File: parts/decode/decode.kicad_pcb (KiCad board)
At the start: 2 copper layers, 37 parts, among them J1 Conn_02x02_Odd_Even, J10 Conn_01x02, J11 Conn_01x02, J12 Conn_01x02, J13 Conn_01x02, J14 Conn_02x04_Odd_Even, J2 Conn_02x04_Odd_Even, J3 Conn_01x02, J4 Conn_01x02, J5 Conn_01x02, J6 Conn_01x02, J7 Conn_01x02, J8 Conn_01x02, J9 Conn_01x02, K1 HK19F, K10 HK19F, K11 HK19F, K2 HK19F, K3 HK19F, K4 HK19F, K5 HK19F, K6 HK19F, K7 HK19F, K8 HK19F, K9 HK19F

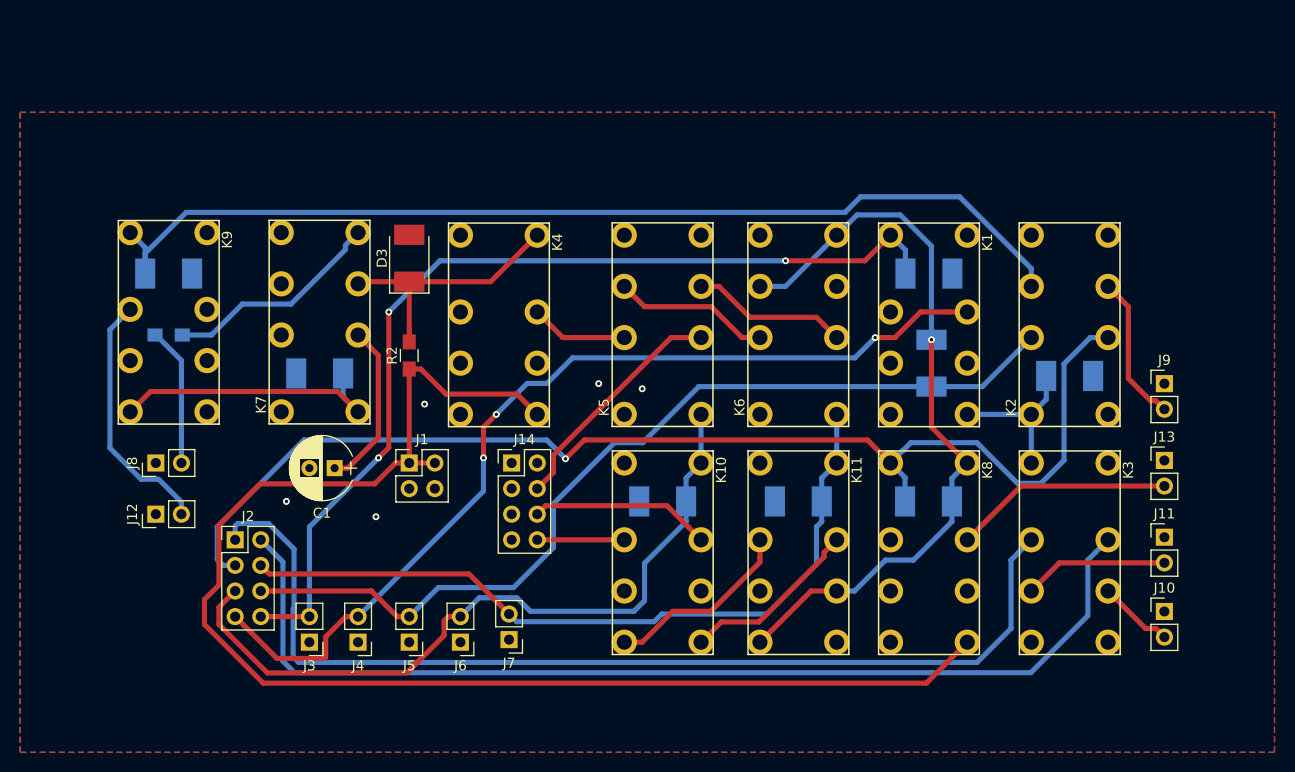
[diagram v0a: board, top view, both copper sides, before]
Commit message: Change opcodes (jumps from rediscovered notes).
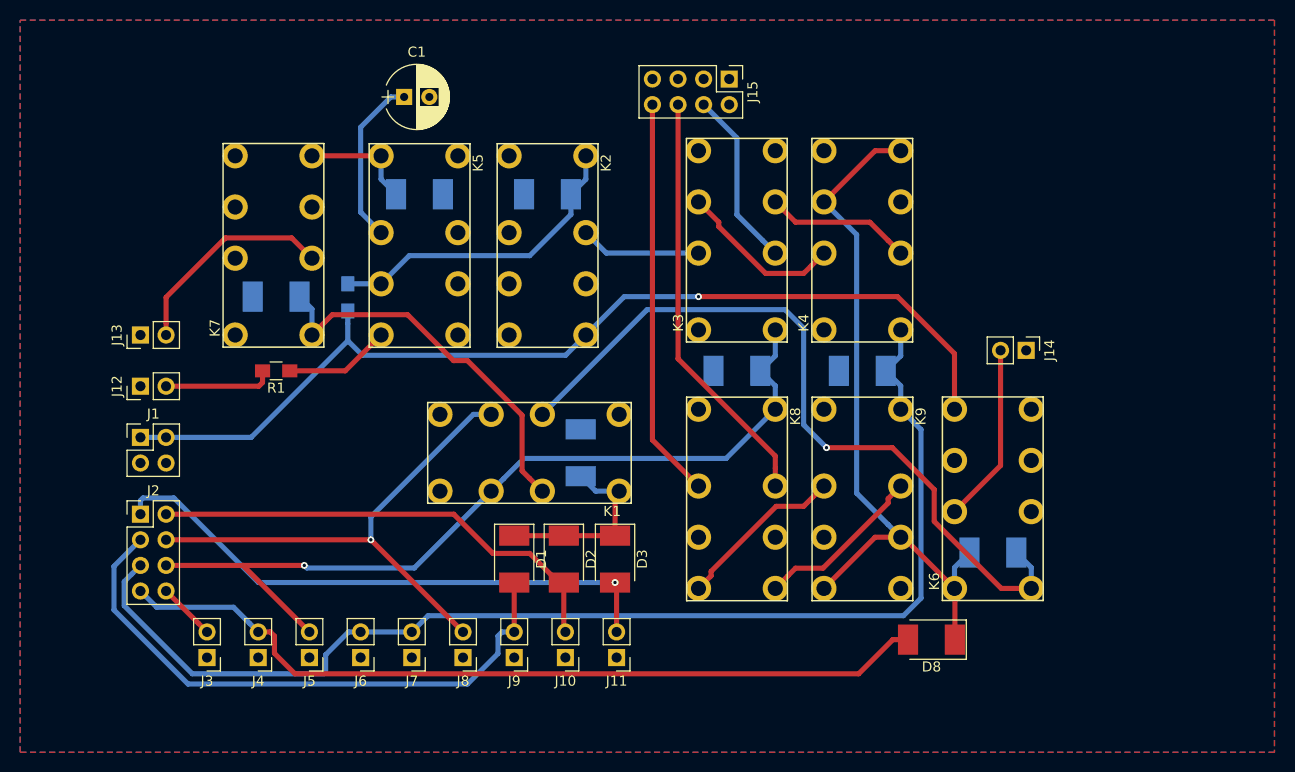
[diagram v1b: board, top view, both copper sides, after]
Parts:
- removed K10, K11: HK19F, hk19f:Relay_DPDT_HK19F
- added D10: D, Diodes_SMD:D_2114, B.Cu at (159.0, 71.6)
- added D11: D, Diodes_SMD:D_2114, B.Cu at (144.8, 81.8)
- added J15: Conn_02x04_Odd_Even, Pin_Headers:Pin_Header_Straight_2x04_Pitch2.54mm, F.Cu at (189.7, 60.2)
- D1, D2, D8, R1: moved to F.Cu
- D7: value D_TVS -> D
- D9: value D -> D_TVS
- J14: value Conn_02x04_Odd_Even -> Conn_01x02; footprint Pin_Headers:Pin_Header_Straight_2x04_Pitch2.54mm -> Pin_Headers:Pin_Header_Straight_1x02_Pitch2.54mm
- R2: moved to B.Cu
- moved J13 102.4 mm to (131.3, 85.6), turned to 90 degrees
- moved D9 86.3 mm to (215.9, 107.2)
- moved K9 71.0 mm to (206.8, 93.0)
- moved J9 70.0 mm to (168.4, 117.6), turned to 180 degrees
- moved D8 66.2 mm to (209.8, 115.8)
- moved J10 59.6 mm to (173.5, 117.6), turned to 180 degrees
- moved J11 55.7 mm to (178.6, 117.6), turned to 180 degrees
- moved D2 53.4 mm to (173.3, 107.8), turned to 270 degrees
- moved J14 52.3 mm to (219.2, 87.1), turned to 270 degrees
- moved K2 51.1 mm to (175.5, 67.8), turned to 270 degrees
- moved D1 50.0 mm to (168.4, 107.8), turned to 270 degrees
- moved K1 42.9 mm to (178.8, 101.1), turned to 180 degrees
- moved K3 42.7 mm to (186.7, 85.1), turned to 90 degrees
- moved D5 39.4 mm to (171.7, 71.6)
- moved C1 37.5 mm to (157.5, 62.0), turned to 0 degrees
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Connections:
- D1 pad 2: GND -> Net-(D1-Pad2)
- D2 pad 1: Net-(D2-Pad1) -> Net-(D1-Pad1)
- D2 pad 2: GND -> Net-(D2-Pad2)
- D3 pad 1: Net-(D3-Pad1) -> Net-(D1-Pad1)
- D3 pad 2: GND -> Net-(D3-Pad2)
- D4 pad 1: Net-(D4-Pad1) -> Net-(D1-Pad1)
- D6 pad 2: Net-(D6-Pad2) -> GND
- D7 pad 1: Net-(D6-Pad1) -> Net-(D7-Pad1)
- D7 pad 2: Net-(D7-Pad2) -> GND
- D8 pad 2: GND -> Net-(D8-Pad2)
- D9 pad 1: Net-(D9-Pad1) -> Net-(D8-Pad1)
- D9 pad 2: GND -> Net-(D9-Pad2)
- J10 pad 2: Net-(J10-Pad2) -> Net-(D2-Pad2)
- J11 pad 2: Net-(J11-Pad2) -> Net-(D3-Pad2)
- J14 pad 2: (no net) -> Net-(J14-Pad2)
- J2 pad 1: Net-(J2-Pad1) -> Net-(D3-Pad2)
- J2 pad 2: Net-(J2-Pad2) -> Net-(D2-Pad2)
- J2 pad 3: Net-(D7-Pad2) -> Net-(D1-Pad2)
- J2 pad 4: Net-(D5-Pad1) -> Net-(J2-Pad4)
- J2 pad 5: Net-(D4-Pad1) -> Net-(D7-Pad1)
- J2 pad 6: Net-(D6-Pad2) -> Net-(D6-Pad1)
- J2 pad 7: Net-(J2-Pad7) -> Net-(D8-Pad2)
- J2 pad 8: Net-(D1-Pad1) -> Net-(J2-Pad8)
- J3 pad 2: Net-(D1-Pad1) -> Net-(J2-Pad8)
- J4 pad 2: Net-(J2-Pad7) -> Net-(D8-Pad2)
- J5 pad 2: Net-(D6-Pad2) -> Net-(D6-Pad1)
- J6 pad 2: Net-(D4-Pad1) -> Net-(D7-Pad1)
- J7 pad 2: Net-(D5-Pad1) -> Net-(D7-Pad1)
- J8 pad 2: Net-(J8-Pad2) -> Net-(J2-Pad4)
- J9 pad 2: Net-(J9-Pad2) -> Net-(D1-Pad2)
- K1 pad 1: GND -> Net-(D1-Pad1)
- K1 pad 11: (no net) -> Net-(J2-Pad4)
- K1 pad 13: (no net) -> Net-(D9-Pad2)
- K1 pad 16: Net-(D1-Pad1) -> GND
- K1 pad 4: Net-(J2-Pad7) -> Net-(D11-Pad1)
- K1 pad 6: (no net) -> Net-(D6-Pad1)
- K1 pad 8: Net-(D2-Pad1) -> (no net)
- K2 pad 1: Net-(D2-Pad1) -> Net-(D5-Pad1)
- K2 pad 11: Net-(J9-Pad2) -> (no net)
- K2 pad 13: Net-(D7-Pad2) -> (no net)
- K2 pad 4: Net-(D6-Pad2) -> Net-(K2-Pad4)
- K2 pad 6: Net-(D9-Pad1) -> GND
- K2 pad 8: (no net) -> +12V
- K3 pad 11: Net-(J11-Pad2) -> Net-(K3-Pad11)
- K3 pad 13: Net-(J2-Pad1) -> Net-(J15-Pad4)
- K3 pad 16: Net-(D2-Pad1) -> Net-(D6-Pad1)
- K3 pad 4: Net-(J2-Pad2) -> Net-(K2-Pad4)
- K3 pad 6: Net-(J10-Pad2) -> Net-(K3-Pad6)
- K4 pad 1: Net-(D3-Pad1) -> GND
- K4 pad 13: (no net) -> Net-(K3-Pad11)
- K4 pad 16: GND -> Net-(D7-Pad1)
- K4 pad 4: Net-(K4-Pad4) -> Net-(K3-Pad6)
- K4 pad 6: GND -> Net-(D8-Pad1)
- K4 pad 8: +12V -> (no net)
- K4 pad 9: (no net) -> Net-(D8-Pad1)
- K5 pad 11: Net-(K5-Pad11) -> Net-(D5-Pad1)
- K5 pad 13: Net-(J14-Pad4) -> Net-(C1-Pad1)
- K5 pad 16: Net-(D4-Pad1) -> Net-(D10-Pad1)
- K5 pad 4: Net-(K4-Pad4) -> (no net)
- K5 pad 6: Net-(K5-Pad6) -> (no net)
- K5 pad 9: (no net) -> Net-(K5-Pad9)
- K6 pad 1: GND -> Net-(D8-Pad1)
- K6 pad 13: Net-(K5-Pad11) -> (no net)
- K6 pad 16: Net-(D5-Pad1) -> Net-(D9-Pad2)
- K6 pad 4: Net-(K5-Pad6) -> Net-(J14-Pad2)
- K6 pad 6: Net-(D6-Pad1) -> GND
- K6 pad 8: (no net) -> +12V
- K6 pad 9: Net-(D6-Pad1) -> (no net)
- K7 pad 11: Net-(D3-Pad1) -> (no net)
- K7 pad 13: Net-(C1-Pad1) -> Net-(J13-Pad2)
- K7 pad 16: Net-(D8-Pad1) -> Net-(D11-Pad1)
- K7 pad 9: Net-(K7-Pad9) -> Net-(D10-Pad1)
- K8 pad 13: (no net) -> Net-(J15-Pad8)
- K8 pad 16: Net-(D7-Pad2) -> GND
- K8 pad 4: Net-(J13-Pad2) -> Net-(J15-Pad6)
- K8 pad 6: GND -> (no net)
- K8 pad 8: +12V -> Net-(K8-Pad8)
- K8 pad 9: (no net) -> Net-(K8-Pad9)
- K9 pad 1: GND -> Net-(D7-Pad1)
- K9 pad 13: Net-(J12-Pad2) -> Net-(K8-Pad9)
- K9 pad 16: Net-(D9-Pad1) -> GND
- K9 pad 4: (no net) -> Net-(K8-Pad8)
- K9 pad 6: (no net) -> Net-(D8-Pad1)
- R1 pad 1: Net-(K7-Pad9) -> Net-(K5-Pad9)
- R1 pad 2: Net-(J8-Pad2) -> Net-(J12-Pad2)
- R2 pad 2: Net-(D3-Pad1) -> Net-(D5-Pad1)
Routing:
- net Net-(D7-Pad1): track 0.00 -> 119.3 mm
- net Net-(D7-Pad2): track 118.2 -> 0.00 mm, vias 1 -> 0
- net Net-(J2-Pad2): track 104.0 -> 0.00 mm
- net Net-(D9-Pad1): track 101.7 -> 0.00 mm
- net Net-(J2-Pad1): track 101.6 -> 0.00 mm
- net Net-(J2-Pad7): track 93.5 -> 0.00 mm, vias 3 -> 0
- net Net-(D6-Pad2): track 91.5 -> 0.00 mm
- net Net-(D8-Pad2): track 0.00 -> 82.0 mm
- net Net-(D1-Pad1): track 95.7 -> 19.0 mm, vias 3 -> 0
- net Net-(D9-Pad2): track 0.00 -> 75.9 mm, vias 0 -> 1
- net Net-(D4-Pad1): track 74.0 -> 0.00 mm
- net Net-(D1-Pad2): track 0.00 -> 58.9 mm
- net Net-(D3-Pad2): track 0.00 -> 57.0 mm, vias 0 -> 1
- net Net-(J2-Pad4): track 0.00 -> 51.7 mm, vias 0 -> 1
- net Net-(D2-Pad2): track 0.00 -> 47.2 mm
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
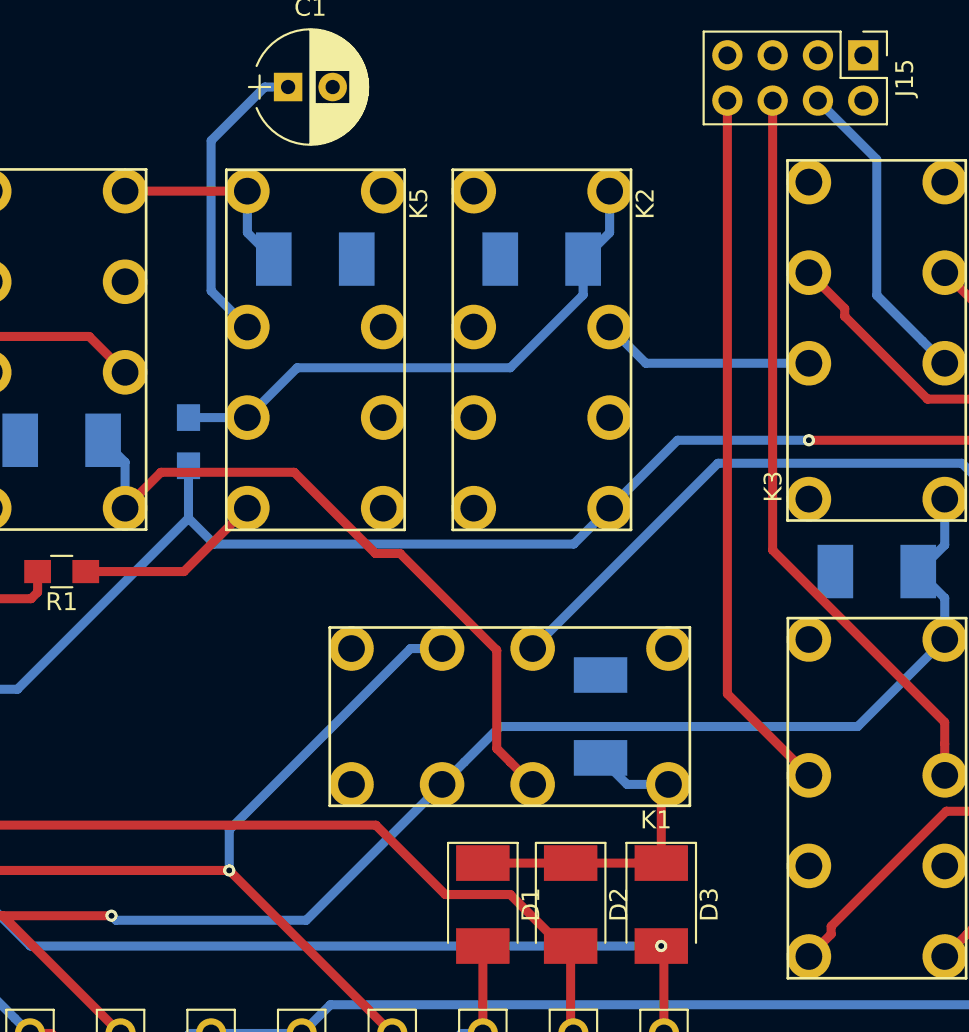
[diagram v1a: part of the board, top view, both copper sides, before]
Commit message: Git-ignore (old) parts directory, commit final changes there.
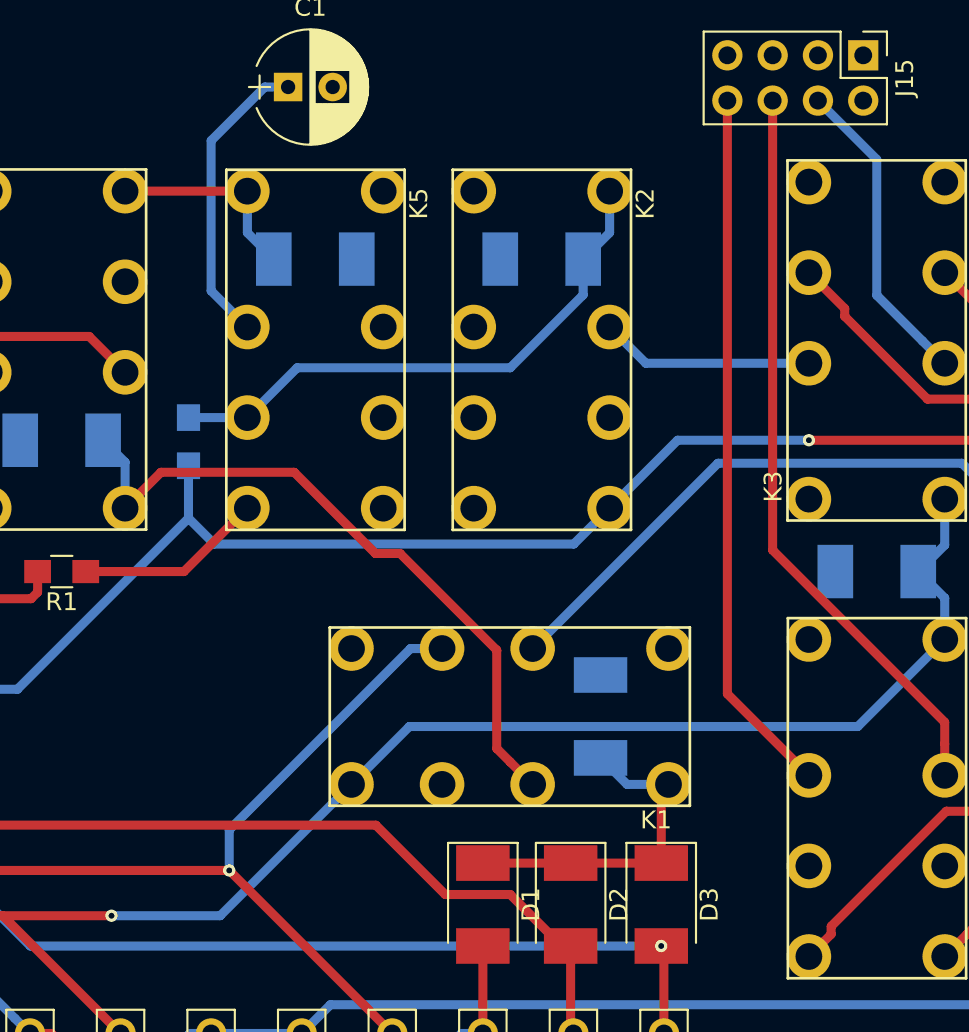
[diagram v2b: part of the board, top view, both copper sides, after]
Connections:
- D6 pad 1: Net-(D6-Pad1) -> Net-(D6-K)
- J15 pad 2: (no net) -> unconnected-(J15-Pin_2-Pad2)
- J2 pad 6: Net-(D6-Pad1) -> Net-(D6-K)
- J5 pad 2: Net-(D6-Pad1) -> Net-(D6-K)
- K1 pad 6: Net-(D6-Pad1) -> unconnected-(K1-Pad6)
- K1 pad 8: (no net) -> Net-(D6-K)
- K1 pad 9: (no net) -> unconnected-(K1-Pad9)
- K2 pad 11: (no net) -> unconnected-(K2-Pad11)
- K2 pad 13: (no net) -> unconnected-(K2-Pad13)
- K2 pad 9: (no net) -> unconnected-(K2-Pad9)
- K3 pad 16: Net-(D6-Pad1) -> Net-(D6-K)
- K3 pad 8: (no net) -> unconnected-(K3-Pad8)
- K3 pad 9: (no net) -> unconnected-(K3-Pad9)
- K4 pad 11: (no net) -> unconnected-(K4-Pad11)
- K4 pad 8: (no net) -> unconnected-(K4-Pad8)
- K5 pad 4: (no net) -> unconnected-(K5-Pad4)
- K5 pad 6: (no net) -> unconnected-(K5-Pad6)
- K5 pad 8: (no net) -> unconnected-(K5-Pad8)
- K6 pad 11: (no net) -> unconnected-(K6-Pad11)
- K6 pad 13: (no net) -> unconnected-(K6-Pad13)
- K6 pad 9: (no net) -> unconnected-(K6-Pad9)
- K7 pad 11: (no net) -> unconnected-(K7-Pad11)
- K7 pad 4: (no net) -> unconnected-(K7-Pad4)
- K7 pad 6: (no net) -> unconnected-(K7-Pad6)
- K7 pad 8: (no net) -> unconnected-(K7-Pad8)
- K8 pad 1: Net-(D6-Pad1) -> Net-(D6-K)
- K8 pad 11: (no net) -> unconnected-(K8-Pad11)
- K8 pad 6: (no net) -> unconnected-(K8-Pad6)
- K9 pad 11: (no net) -> unconnected-(K9-Pad11)
- K9 pad 8: (no net) -> unconnected-(K9-Pad8)
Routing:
- net Net-(D6-Pad1): track 85.5 -> 0.00 mm, vias 1 -> 0
- net Net-(D6-K): track 0.00 -> 85.3 mm, vias 0 -> 1
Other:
- net class Default removed
